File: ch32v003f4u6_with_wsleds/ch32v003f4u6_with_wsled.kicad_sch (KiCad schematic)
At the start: 30 parts, among them J2 PGM, J4 USB_C_Receptacle_USB2.0, J5 HOLE, J6 HOLE, U1 CH32V003F4U6, U2 3.3vReg

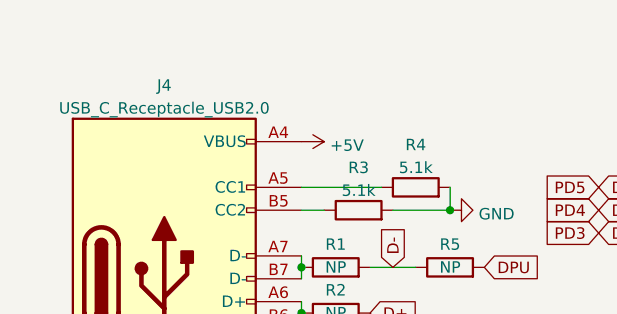
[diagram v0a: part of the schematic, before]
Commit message: Bump to what was ordered.
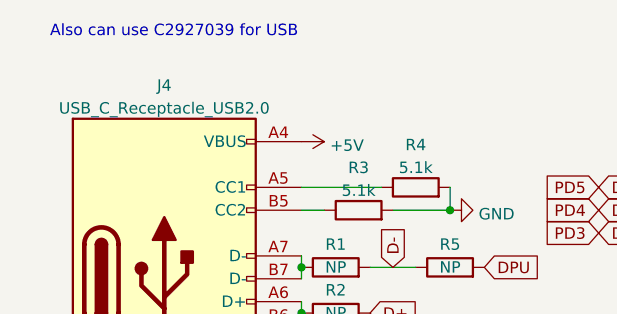
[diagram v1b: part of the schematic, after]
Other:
- note added: "Also can use C2927039 for USB"
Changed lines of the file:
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@@
     (stroke (width 0) (type default) (color 0 0 0 0))
+  )
+  (text "Also can use C2927039 for USB" (at 21.59 20.32 0)
+    (effects (font (size 1.27 1.27)) (justify left bottom))
   )
   (global_label "PC5" (shape input) (at 187.96 114.3 180) (fields_autoplaced)
